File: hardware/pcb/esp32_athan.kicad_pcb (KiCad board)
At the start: 2 copper layers, 50 x 55.6 mm, 37 parts, among them J1 USB_C_Receptacle_PowerOnly_6P, J3 Speaker, J4 OLED, J5 Relay, J6 PROG, SW1 Next, SW2 Select, U1 ESP32-S3-WROOM-1-N16R8, U3 AMS1117-3.3, U4 MAX98357A

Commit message: update schematic and layout with new resistance and new 5-way button instead of select,next
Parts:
- removed QR*****: QRCode_esp32_athan_p5, Library:QRCode_esp32_athan_p5
- removed QR*****: QRCode_esp32_athan, Library:QRCode_esp32_athan
- removed SW2: Select, Button_Switch_THT:SW_SPST_Omron_B3F-40xx
- R5: value 560k -> 4.7k
- SW1: value Next -> SKRHABE010; footprint Button_Switch_THT:SW_SPST_Omron_B3F-40xx -> SKRHABE010:SW-SMD_SKRHABE010
- moved SW1 12.0 mm to (81.6, 88.1), turned to -135 degrees
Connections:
- SW1 pad 1: BTN_NEXT -> BTN_UP
- SW1 pad 2: GND -> BTN_SELECT
- U1 pad 18: BTN_NEXT -> BTN_DOWN
- U1 pad 22: unconnected-(U1-IO14-Pad22) -> BTN_UP
- U1 pad 23: unconnected-(U1-IO21-Pad23) -> BTN_LEFT
- U1 pad 24: unconnected-(U1-IO47-Pad24) -> BTN_RIGHT
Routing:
- net BTN_RIGHT: track 0.00 -> 61.5 mm, vias 0 -> 1
- net BTN_UP: track 0.00 -> 59.0 mm, vias 0 -> 3
- net BTN_LEFT: track 0.00 -> 52.0 mm, vias 0 -> 3
- net BTN_DOWN: track 0.00 -> 34.7 mm, vias 0 -> 1
- net BTN_NEXT: track 33.8 -> 0.00 mm, vias 1 -> 0
- net BTN_SELECT: track 30.2 -> 24.6 mm, vias 1 -> 3
- net GND: track 9.56 -> 12.1 mm, vias 98 -> 100

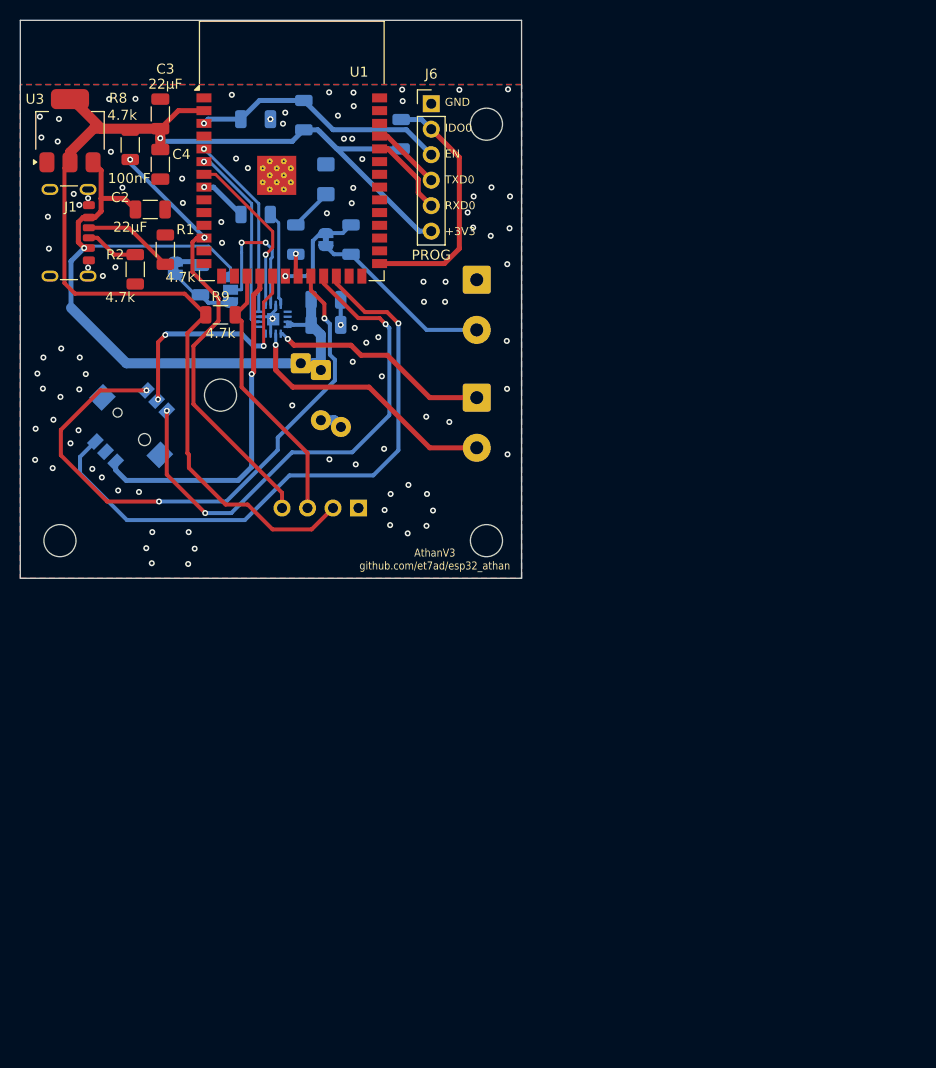
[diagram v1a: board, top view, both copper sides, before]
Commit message: Add colour TFT build option, screen settings and the drawn PCB
Display
- The display is chosen at build time: display_type oled|tft, or --display in
  build_firmware.sh and flash_firmware.sh. Each display's code lives in
  firmware/displays/{oled,tft}.yaml. A TFT build has its own release files and
  manifest (manifest-tft.json), so a clock only updates to its own build.
- 240x240 ST7789 TFT (mipi_spi):
  - a ring clock with seconds, flashing 500/500 ms in the last minute
    before an athan;
  - a prayer strip, and mute icons for prayers whose athan is off;
  - a two-pane colour menu with Material Symbols icons;
  - Screen Colour (5 palettes) and a colour Wi-Fi setup screen.
- The OLED drawing is unchanged, behind ATHAN_DISPLAY_TFT. Both displays read
  the menu from one Frame (menu_frame.h).

Screen settings (both displays, menu and web page)
- Brightness 0-100 % (0 % = dark until a key).
- Screen at Night: Off / Dim / Dark, with Night From and Night Until.
- While the screen is dark, a key lights it, dim, for 2 min with a countdown.
- The tick and night windows can end at a prayer (From Maghrib/Isha, Until
  Fajr/Dhuhr), worked out from each day's times (day_window.h, host-tested).
  The window rows are now choices confirmed with Select, with a caption
  previewing the result.

Audio
- Fix a flash preview that kept playing after leaving its menu row: a preview
  still waiting to start is now dropped (cancel_pending_slot_preview_).
- The menu tones are mono 16-bit WAV (no decoding, no MP3 padding). Stored
  sounds stay MP3.

Hardware
- PCB drawn in KiCad: OLED header J4, TFT header J7, 5-way switch footprints
  and 3D models, renders and a STEP export.

README
- 1.1: the clock joins 2.4 GHz Wi-Fi only.
- 1.2 Screen: the OLED's timetable screen and its marks, the colour screen
  (ring, strip, last-minute flash, athan colour, Screen Colour), and the
  dark screen waking on a key.
- 1.3 Menu: two panes, short names, the new rows (Tick From/Until,
  Brightness, Screen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
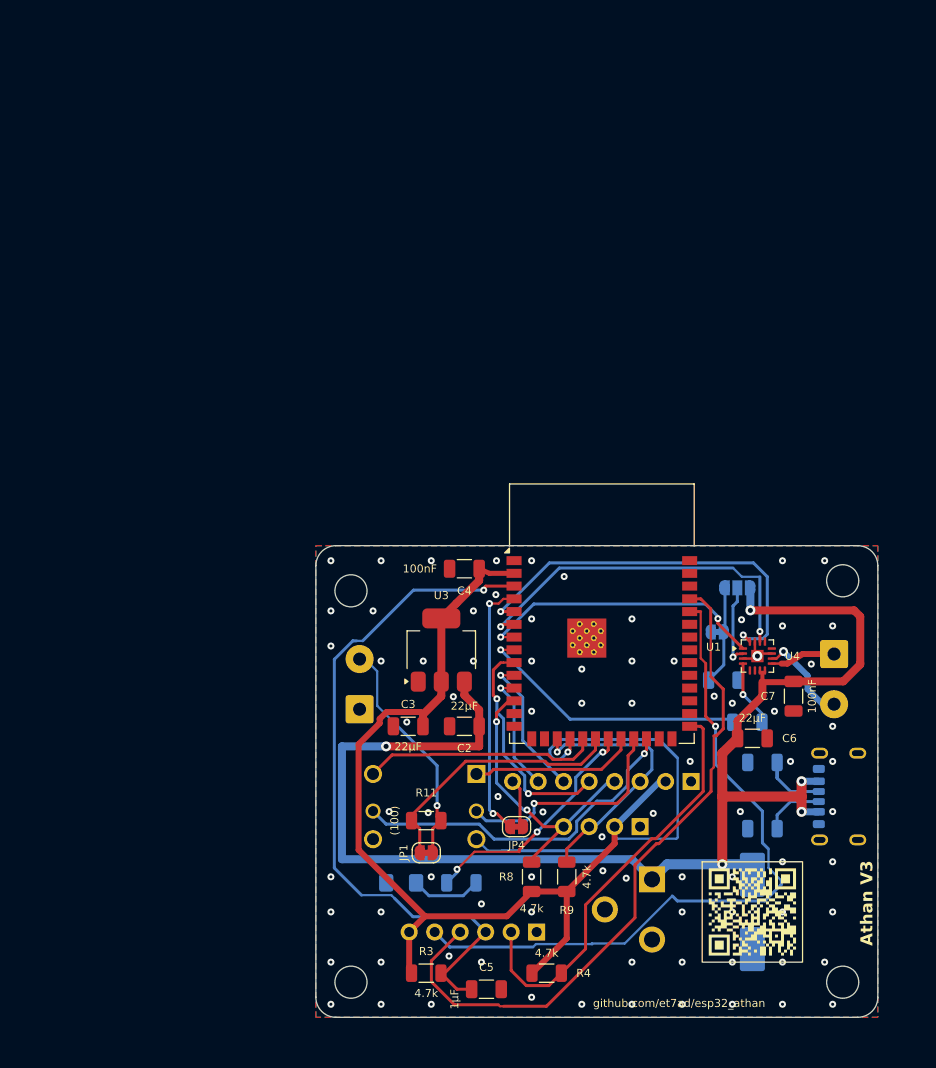
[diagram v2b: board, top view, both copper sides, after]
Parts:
- removed SW1: SKRHABE010, SKRHABE010:SW-SMD_SKRHABE010
- added J2: Barrel_Jack, Connector_BarrelJack:BarrelJack_CUI_PJ-102AH_Horizontal, B.Cu at (133.5, 133.2)
- added J7: TFT, Connector_PinHeader_2.54mm:PinHeader_1x08_P2.54mm_Vertical, B.Cu at (137.4, 123.5)
- added JP4: SolderJumper_2_Bridged, Jumper:SolderJumper-2_P1.3mm_Bridged_RoundedPad1.0x1.5mm, F.Cu at (120.0, 128.0)
- added QR*****: QRCode_esp32_athan_p3, Library:QRCode_esp32_athan_p3, F.Cu at (143.5, 136.5)
- added QR*****: QRCode_esp32_athan_p5, Library:QRCode_esp32_athan_p5, B.Cu at (128.0, 109.4)
- added U2: SKQUAAA010, SKQUAAA010:SKQUAAA010, B.Cu at (116.0, 129.2)
- C1: footprint Capacitor_THT:CP_Radial_D10.0mm_P5.00mm_P7.50mm -> Capacitor_SMD:CP_Elec_8x10.5
- C5, C6, C7, JP1, R11, R3, R4, U4: moved to F.Cu
- J1, J6, R1, R2: moved to B.Cu
- moved J1 96.9 mm to (153.2, 125.0)
- moved C5 89.7 mm to (117.0, 144.2)
- moved R3 86.4 mm to (111.0, 142.6), turned to 0 degrees
- moved R4 84.8 mm to (123.0, 142.6), turned to 0 degrees
- moved R2 83.7 mm to (144.5, 128.2), turned to 180 degrees
- moved J6 83.2 mm to (122.0, 138.5), turned to 90 degrees
- moved R8 83.2 mm to (121.5, 133.0), turned to 90 degrees
- moved R1 78.4 mm to (144.5, 121.6), turned to 180 degrees
- moved D1 70.5 mm to (108.5, 133.6), turned to 0 degrees
- moved R5 70.4 mm to (143.0, 117.6)
- moved C1 69.0 mm to (143.5, 136.5)
- moved R10 66.2 mm to (114.5, 133.6), turned to 0 degrees
- moved C3 65.8 mm to (109.2, 118.0), turned to 180 degrees
- moved R9 65.8 mm to (125.0, 133.0), turned to 90 degrees
- moved R7 65.6 mm to (140.6, 113.4), turned to 0 degrees
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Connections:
- net I2C_SCL renamed DISP_SCL
- net I2C_SDA renamed DISP_SDA
- U1 pad 10: unconnected-(U1-IO17-Pad10) -> DISP_DC
- U1 pad 11: unconnected-(U1-IO18-Pad11) -> DISP_CS
- U1 pad 4: unconnected-(U1-IO4-Pad4) -> DISP_BL
- U1 pad 9: unconnected-(U1-IO16-Pad9) -> DISP_RES
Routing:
- net +5V: track 75.8 -> 140.2 mm, vias 1 -> 5
- net TXD0: track 6.97 -> 68.8 mm
- net RXD0: track 8.28 -> 69.8 mm, vias 0 -> 1
- net EN: track 25.8 -> 69.5 mm
- net BTN_UP: track 59.0 -> 16.5 mm, vias 3 -> 0
- net BTN_LEFT: track 52.0 -> 22.8 mm, vias 3 -> 1
- net +3V3: track 124.7 -> 96.1 mm, vias 1 -> 0
- net BTN_RIGHT: track 61.5 -> 34.7 mm
- net DISP_BL: track 0.00 -> 25.9 mm, vias 0 -> 2
- net DISP_RES: track 0.00 -> 22.7 mm, vias 0 -> 2
- net AMP_SD: track 4.82 -> 27.4 mm
- net LED: track 2.40 -> 23.9 mm, vias 1 -> 3
- net I2S_BCLK: track 18.5 -> 39.9 mm, vias 1 -> 2
- net I2S_LRCLK: track 18.9 -> 36.5 mm, vias 1 -> 2
- net /SPK-: track 26.9 -> 9.46 mm
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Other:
- board size 50 x 55.6 mm -> 56 x 47 mm
- board text added: "12dB"
- board text added: "3V3"
- board text added: "5V DC, centre +"
- board text added: "6dB"
- board text added: "Athan V3"
- board text added: "BL"
- board text added: "COM"
- board text added: "CS"
- board text added: "DC"
- board text added: "DN"
- board text added: "EN"
- board text added: "GAIN open = 9 dB"
- board text added: "GND"
- board text added: "IO0"
- board text added: "LT"
- board text added: "OLED"
- board text added: "PROG"
- board text added: "RES"
- board text added: "RLY+"
- board text added: "RT"
- board text added: "RX"
- board text added: "SCL"
- board text added: "SDA"
- board text added: "SEL"
- board text added: "SPK+"
- board text added: "SPK-"
- board text added: "TFT"
- board text added: "TX"
- board text added: "UP"
- board text added: "VCC"
- board text added: "github.com/et7ad/esp32_athan"
- board text removed: "+ -"
- board text removed: "- +"
- board text removed: "AthanV3 github.com/et7ad/esp32_athan"
- board text removed: "GND 3V3 SCL SDA"
- board text removed: "GND IDO0 EN TXD0 RXD0 +3V3"

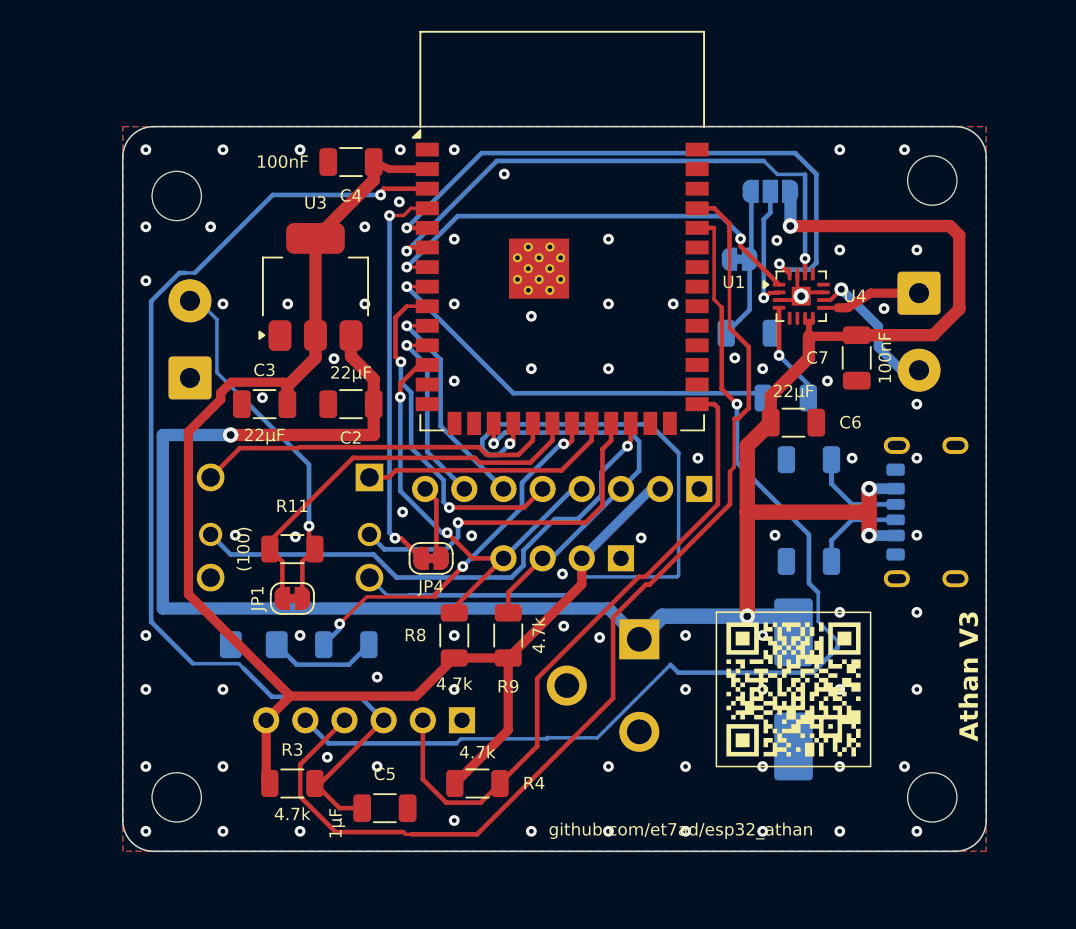
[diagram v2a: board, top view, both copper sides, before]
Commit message: Lists of any length, full code review fixes, 44.1 kHz sounds, PCB v5
Sound lists
- The suggested lists (athan, Fajr, tawashih, tick) can have any number of
  entries, numbered in file order ("2. Abdul Basit") in the menu, on /audio
  and on the web page; long names wrap or shorten to fit both displays.
- /audio: one form per sound, with its whole list in a dropdown (the one in
  use marked with a check mark) and Preview / Download buttons; the status
  bar says "downloaded and in use" and offers Reload page when the lists change.
- Radio stays at 10 stations; README shows how to add one from mp3quran.net,
  with screenshots.

Screen and windows
- Tick window: from Fajr or Dhuhr until Maghrib or Isha; night window the
  other way round. An end a window no longer offers becomes an hour at boot.
- Screen at Night: Normal (same as by day) / Dim / Turned off. Normal ignores
  the night window; Dim is never brighter than by day.
- New Night Window line on the web page; both window lines update within
  100 ms of a change.

TFT clock face
- Most seconds redraw only the seconds (about 2.5 ms instead of a 50 ms whole
  face). The whole face is redrawn every 30 s, at each minute, on any change,
  and every second in the last minute.
- The ring is drawn in one pass (tft::ring), pixel-identical to a plain scan
  over 5,820 host-tested cases.
- Frames follow the clock's own second. The last-minute flash is exactly
  500 ms lit / 500 ms dark (measured on the prototype).

Fixes from a full code review (tested on the prototype)
- An upload that broke off left every download "Busy" until a restart.
  It is now freed after 20 s.
- Saving a sound froze the clock for seconds and restarted the I2S speaker
  under the radio. Erases now go block by block with pauses, the radio
  pauses for the write, and the read-back check runs on the worker.
- A stored sound whose end the player lost could not be stopped by the
  5 s bound. Its resampler is now stopped. Joined or damaged MP3 uploads
  a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
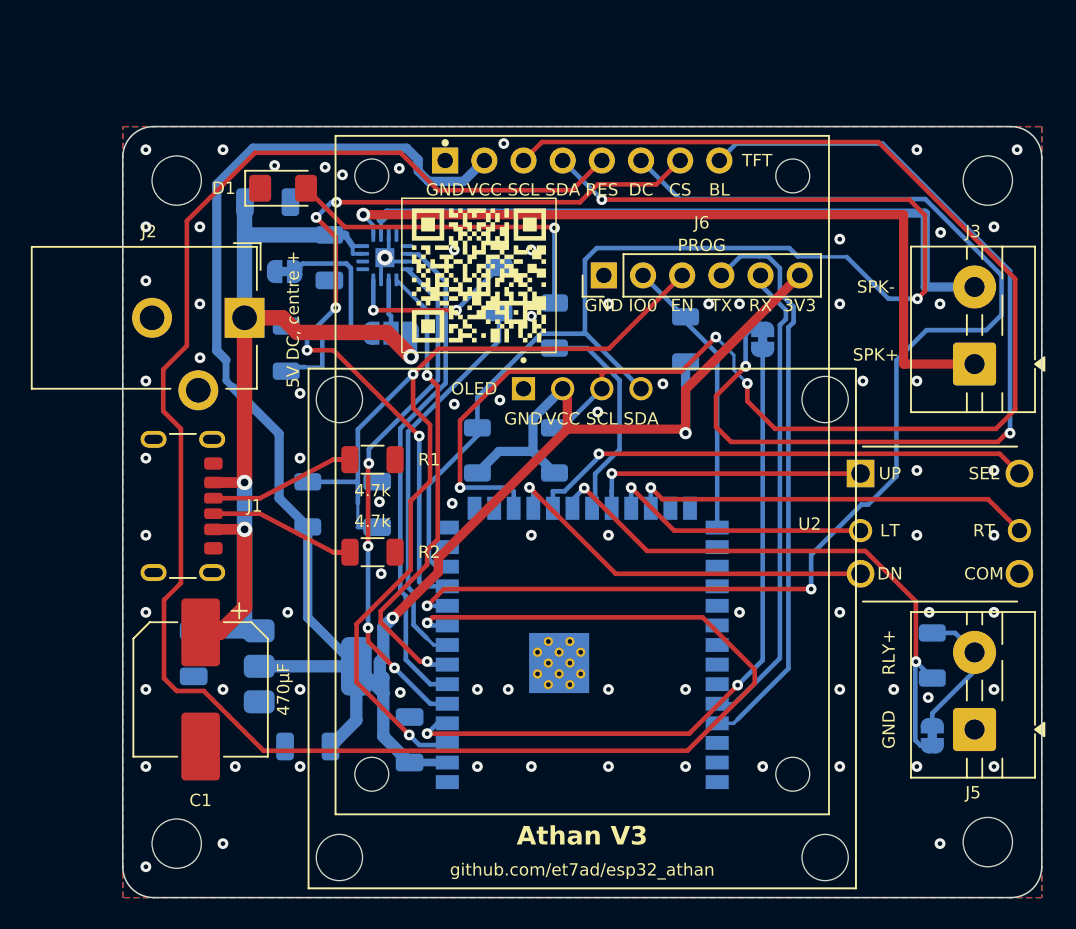
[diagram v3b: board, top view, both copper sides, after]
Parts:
- removed J4: OLED, Connector_PinHeader_2.54mm:PinHeader_1x04_P2.54mm_Vertical
- removed J7: TFT, Connector_PinHeader_2.54mm:PinHeader_1x08_P2.54mm_Vertical
- removed QR*****: QRCode_esp32_athan_p3, Library:QRCode_esp32_athan_p3
- removed QR*****: QRCode_esp32_athan_p5, Library:QRCode_esp32_athan_p5
- added DS1: OLED, Library:LCD_OLED_128X64_1.3_I2C, F.Cu at (129.8, 132.6)
- added DS2: TFT, Library:Display_TFT_1.54in_ST7789_240x240_8pin, F.Cu at (129.8, 102.2)
- added SYM1: qrcode_front, Library:QRCode_esp32_athan_p3, F.Cu at (123.1, 109.7)
- added SYM2: qrcode_back, Library:QRCode_esp32_athan_p3, B.Cu at (145.6, 135.3)
- C1, D1, J1, J2, J3, J5, J6, R1, R2, U2: moved to F.Cu
- C2, C3, C4, C5, C6, C7, JP1, JP4, R11, R3, R4, R8, R9, U1, U3, U4: moved to B.Cu
- moved J5 55.8 mm to (155.2, 139.1)
- moved J1 50.4 mm to (102.8, 124.6)
- moved JP1 42.4 mm to (152.5, 139.5), turned to 90 degrees
- moved R11 42.1 mm to (152.5, 134.3), turned to 90 degrees
- moved C1 38.5 mm to (105.0, 136.5)
- moved C4 37.7 mm to (118.6, 139.8), turned to 90 degrees
- moved C6 37.0 mm to (109.4, 104.9)
- moved C7 34.8 mm to (113.4, 108.5)
- moved J2 33.0 mm to (107.9, 112.4), turned to -90 degrees
- moved U2 31.9 mm to (147.8, 129.0), turned to 0 degrees
- moved R4 31.8 mm to (136.5, 113.8), turned to 90 degrees
- moved U1 30.5 mm to (129.8, 137.2)
- moved J6 30.3 mm to (131.2, 109.7)
- moved R7 30.0 mm to (110.6, 114.4), turned to 90 degrees
- moved D1 29.7 mm to (110.4, 104.0)
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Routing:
- net DISP_RES: track 22.7 -> 128.9 mm, vias 2 -> 1
- net DISP_SCL: track 26.3 -> 101.3 mm, vias 1 -> 3
- net +5V: track 140.2 -> 67.2 mm, vias 5 -> 3
- net DISP_DC: track 14.5 -> 81.1 mm, vias 1 -> 2
- net DISP_SDA: track 29.5 -> 85.6 mm
- net Net-(DS2-Pin_8): track 4.93 -> 61.0 mm, vias 0 -> 2
- net /SPK+: track 6.48 -> 50.9 mm, vias 0 -> 1
- net DISP_CS: track 12.2 -> 56.2 mm, vias 1 -> 5
- net +3V3: track 96.1 -> 139.2 mm, vias 0 -> 2
- net RXD0: track 69.8 -> 31.0 mm, vias 1 -> 0
- net /SPK-: track 9.46 -> 44.5 mm, vias 1 -> 0
- net TXD0: track 68.8 -> 37.2 mm
- net IO0: track 41.9 -> 18.4 mm
- net BTN_DOWN: track 47.1 -> 25.2 mm
- net DISP_BL: track 25.9 -> 45.5 mm
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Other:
- board size 56 x 47 mm -> 59.6 x 50 mm

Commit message: Guides for owners and builders, update mark, JLCPCB assembly files
Docs
- README is now a short landing page: the board picture (front and back,
  to scale, with the 1.54" screen showing the clock), the note for
  version 2 owners, why the prayer times come from this repository, then
  the 2.4 GHz warning, first setup, the joystick, the web page, updates
  and links to the guides.
- New guides/: using.md (setup, screen, keys and menu, web page, sounds,
  radio, prayer times, updates), building.md (prototype, firmware build
  and flash, the board, acceptance checklist), maintaining.md (prayer
  times, sounds, stations, releases) and jlcpcb_assembly.md (ordering the
  board assembled).
- HARDWARE.md rewritten from the KiCad netlist and part positions: power,
  pin map, amplifier, switch, parts list with LCSC numbers and prices,
  layout, enclosure. max98357a_amplifier.md uses the board's part numbers
  and its gain solder jumpers.
- References in the docs, scripts and comments point at the new guides
  and HARDWARE.md sections.
- The Home Assistant key is in using.md section 4. check_docs.py fails if
  it differs from athan.yaml's, and reads the mosque table from using.md.

Firmware updates
- Checked once after each start (30 s after Wi-Fi first connects) and
  daily at 03:00, instead of every 6 h. ESPHome's own start-up check gave
  up when Wi-Fi took more than a minute.
- Never installed by itself (firmware_rules.md 3.2). An update found shows
  as a small up arrow among the status marks on both screens while
  online, and the menu's Update row offers Install. README and using.md
  section 8 show the mark.
- The Update row reads the update's own state: an update found by any
  check shows as Install, and a failed install offers it again ("Install
  failed: try again") instead of staying on "Installing...".
- Firmware Version says "installing 3.0.1 failed, try again" after a
  failed install, not "no release found on GitHub, or no internet".
- Checked: esphome config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
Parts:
- R10: value 330 -> 100
